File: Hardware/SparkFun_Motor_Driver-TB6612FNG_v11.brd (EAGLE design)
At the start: 20.3 x 20.3 mm, 14 parts, among them U1 TB6612FNG

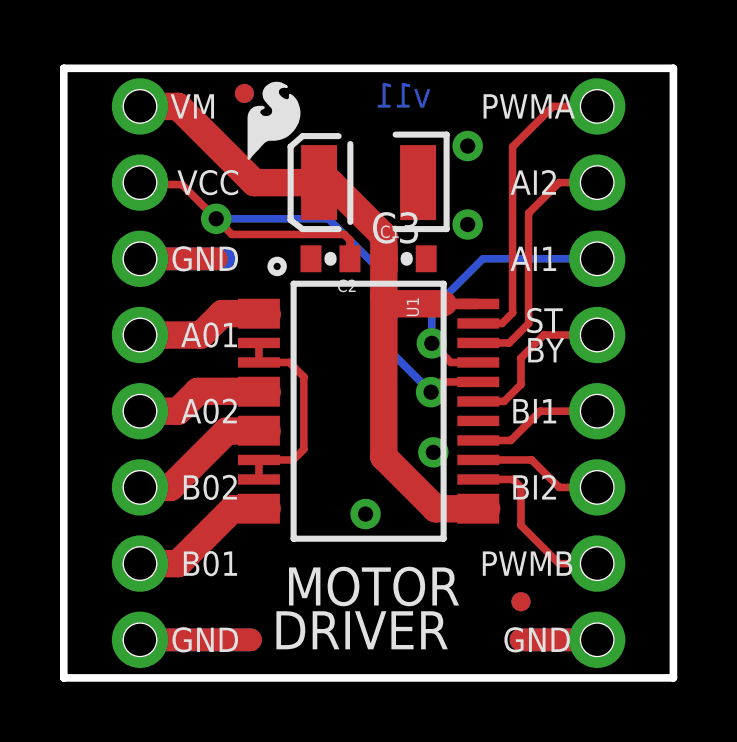
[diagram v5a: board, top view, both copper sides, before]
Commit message: Changed cap parts and added measures
-Replaced 0603 caps with caps from the sparkfun-capacitors lbr
-Replaced 10uf cap with cap from the sparkfun-capacitors lbr
-added measures to the design
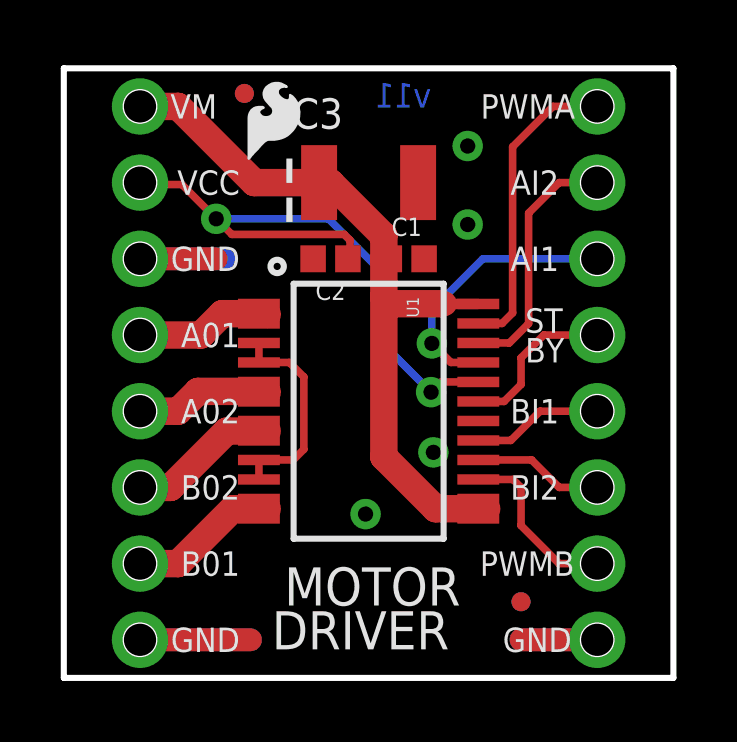
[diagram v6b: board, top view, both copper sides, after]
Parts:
- C1, C2: device SparkFun:0402-CAP -> SparkFun-Capacitors:0402
- C3: value 10uf , 20V -> 10uF; device SparkFun:EIA3528 -> SparkFun-Capacitors:EIA3528
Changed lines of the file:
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@@
 <setting verticaltext="up"/>
 </settings>
-<grid distance="0.05" unitdist="inch" unit="inch" style="lines" multiple="1" display="yes" altdistance="0.005" altunitdist="inch" altunit="inch"/>
+<grid distance="0.05" unitdist="inch" unit="inch" style="lines" multiple="1" display="yes" altdistance="0.0025" altunitdist="inch" altunit="inch"/>
 <layers>
 <layer number="1" name="Top" color="4" fill="1" visible="yes" active="yes"/>
@@
 <layer number="20" name="Dimension" color="15" fill="1" visible="yes" active="yes"/>
 <layer number="21" name="tPlace" color="16" fill="1" visible="yes" active="yes"/>
-<layer number="22" name="bPlace" color="14" fill="1" visible="no" active="yes"/>
+<layer number="22" name="bPlace" color="14" fill="1" visible="yes" active="yes"/>
 <layer number="23" name="tOrigins" color="15" fill="1" visible="yes" active="yes"/>
-<layer number="24" name="bOrigins" color="15" fill="1" visible="no" active="yes"/>
-<layer number="25" name="tNames" color="7" fill="1" visible="yes" active="yes"/>
+<layer number="24" name="bOrigins" color="15" fill="1" visible="yes" active="yes"/>
+<layer number="25" name="tNames" color="7" fill="1" visible="no" active="yes"/>
 <layer number="26" name="bNames" color="7" fill="1" visible="no" active="yes"/>
 <layer number="27" name="tValues" color="7" fill="1" visible="no" active="yes"/>
@@
 <layer number="42" name="bRestrict" color="1" fill="10" visible="no" active="yes"/>
 <layer number="43" name="vRestrict" color="2" fill="10" visible="no" active="yes"/>
-<layer number="44" name="Drills" color="7" fill="1" visible="yes" active="yes"/>
+<layer number="44" name="Drills" color="7" fill="1" visible="no" active="yes"/>
 <layer number="45" name="Holes" color="7" fill="1" visible="yes" active="yes"/>
 <layer number="46" name="Milling" color="3" fill="1" visible="no" active="yes"/>
-<layer number="47" name="Measures" color="7" fill="1" visible="no" active="yes"/>
-<layer number="48" name="Document" color="7" fill="1" visible="no" active="yes"/>
-<layer number="49" name="Reference" color="13" fill="1" visible="no" active="yes"/>
+<layer number="47" name="Measures" color="7" fill="1" visible="yes" active="yes"/>
+<layer number="48" name="Document" color="7" fill="1" visible="yes" active="yes"/>
+<layer number="49" name="Reference" color="13" fill="1" visible="yes" active="yes"/>
 <layer number="50" name="dxf" color="7" fill="1" visible="no" active="yes"/>
-<layer number="51" name="tDocu" color="6" fill="1" visible="no" active="yes"/>
+<layer number="51" name="tDocu" color="6" fill="1" visible="yes" active="yes"/>
 <layer number="52" name="bDocu" color="7" fill="1" visible="no" active="yes"/>
 <layer number="53" name="tGND_GNDA" color="7" fill="9" visible="no" active="no"/>
@@
 <layer number="225" name="225bmp" color="7" fill="1" visible="no" active="yes"/>
 <layer number="226" name="226bmp" color="7" fill="1" visible="no" active="yes"/>
-<layer number="227" name="LAYER_2" color="11" fill="1" visible="no" active="yes"/>
-<layer number="228" name="LAYER_3" color="10" fill="1" visible="no" active="yes"/>
-<layer number="229" name="LAYER_4" color="14" fill="1" visible="no" active="yes"/>
-<layer number="230" name="LAYER_5" color="12" fill="1" visible="no" active="yes"/>
-<layer number="231" name="LAYER_6" color="9" fill="1" visible="no" active="yes"/>
+<layer number="227" name="LAYER_2" color="11" fill="1" visible="yes" active="yes"/>
+<layer number="228" name="LAYER_3" color="10" fill="1" visible="yes" active="yes"/>
+<layer number="229" name="LAYER_4" color="14" fill="1" visible="yes" active="yes"/>
+<layer number="230" name="LAYER_5" color="12" fill="1" visible="yes" active="yes"/>
+<layer number="231" name="LAYER_6" color="9" fill="1" visible="yes" active="yes"/>
 <layer number="232" name="Eagle3D_PG2" color="7" fill="1" visible="no" active="yes"/>
 <layer number="233" name="Eagle3D_PG3" color="7" fill="1" visible="no" active="yes"/>
@@
 <board>
 <plain>
-<wire x1="0" y1="0" x2="20.32" y2="0" width="0.254" layer="20"/>
-<wire x1="20.32" y1="0" x2="20.32" y2="20.32" width="0.254" layer="20"/>
-<wire x1="20.32" y1="20.32" x2="0" y2="20.32" width="0.254" layer="20"/>
-<wire x1="0" y1="20.32" x2="0" y2="0" width="0.254" layer="20"/>
+<wire x1="0" y1="0" x2="20.32" y2="0" width="0.2032" layer="20"/>
+<wire x1="20.32" y1="0" x2="20.32" y2="20.32" width="0.2032" layer="20"/>
+<wire x1="20.32" y1="20.32" x2="0" y2="20.32" width="0.2032" layer="20"/>
+<wire x1="0" y1="20.32" x2="0" y2="0" width="0.2032" layer="20"/>
 <text x="3.5814" y="19.558" size="1.016" layer="22" font="vector" ratio="15" rot="MR180">VM</text>
 <text x="3.5814" y="17.018" size="1.016" layer="22" font="vector" ratio="15" rot="MR180">VCC</text>
@@
 <text x="-7.62" y="-15.24" size="1.778" layer="51" font="vector" ratio="10">Revised by:</text>
 <text x="12.7" y="-15.24" size="1.778" layer="51" font="vector" ratio="10">Eric Orosel</text>
+<dimension x1="0" y1="20.32" x2="20.32" y2="20.32" x3="10.16" y3="26.67" textsize="1.778" textratio="15" layer="47" unit="inch"/>
+<dimension x1="2.54" y1="19.05" x2="17.78" y2="19.05" x3="10.16" y3="22.86" textsize="1.778" textratio="15" layer="47" unit="inch"/>
+<dimension x1="0" y1="20.32" x2="0" y2="0" x3="-6.35" y3="10.16" textsize="1.778" textratio="15" layer="47" unit="inch"/>
+<dimension x1="0" y1="20.32" x2="0" y2="19.05" x3="-2.54" y3="19.685" textsize="1.778" textratio="15" layer="47" unit="inch"/>
 </plain>
 <attributes>
@@
 <attribute name="VALUE" value="TB6612FNG" x="10.16" y="8.89" size="1.778" layer="27" rot="R270" display="off"/>
 </element>
-<element name="C1" library="SparkFun" package="0402-CAP" value="0.1uF" x="11.43" y="13.97"/>
-<element name="C2" library="SparkFun" package="0402-CAP" value="0.1uF" x="8.89" y="13.97" rot="R180"/>
-<element name="C3" library="SparkFun" package="EIA3528" value="10uf , 20V" x="10.16" y="16.51" smashed="yes" rot="R180">
-<attribute name="NAME" x="11.91" y="15.51" size="1.016" layer="25" rot="R180"/>
-<attribute name="VALUE" x="14.704" y="24.2" size="1.016" layer="27" rot="R180"/>
+<element name="C1" library="SparkFun-Capacitors" package="0402" value="0.1uF" x="11.43" y="13.97">
+<attribute name="PROD_ID" value="CAP-12416" x="11.43" y="13.97" size="1.778" layer="27" display="off"/>
+<attribute name="VALUE" value="0.1uF" x="11.43" y="13.97" size="1.778" layer="27" display="off"/>
+</element>
+<element name="C2" library="SparkFun-Capacitors" package="0402" value="0.1uF" x="8.89" y="13.97" rot="R180">
+<attribute name="PROD_ID" value="CAP-12416" x="8.89" y="13.97" size="1.778" layer="27" rot="R180" display="off"/>
+<attribute name="VALUE" value="0.1uF" x="8.89" y="13.97" size="1.778" layer="27" rot="R180" display="off"/>
+</element>
+<element name="C3" library="SparkFun-Capacitors" package="EIA3528" value="10uF" x="10.16" y="16.51" smashed="yes" rot="R180">
+<attribute name="NAME" x="9.3065" y="19.32" size="1.016" layer="25" rot="R180"/>
+<attribute name="VALUE" value="10uF" x="13.6245" y="19.3105" size="1.016" layer="27" rot="R180"/>
+<attribute name="PROD_ID" value="CAP-08063" x="10.16" y="16.51" size="1.778" layer="27" rot="R180" display="off"/>
 </element>
 <element name="JP1" library="Testing" package="1X08_OFFSET_REDUCED" value="" x="2.54" y="1.27" smashed="yes" rot="R90">
@@
 <wire x1="10.668" y1="14.732" x2="8.89" y2="16.51" width="0.9144" layer="1"/>
 <wire x1="10.668" y1="13.97" x2="10.668" y2="14.732" width="0.9144" layer="1"/>
-<wire x1="10.668" y1="13.97" x2="10.78" y2="13.97" width="0.254" layer="1"/>
+<wire x1="10.668" y1="13.97" x2="10.85" y2="13.97" width="0.254" layer="1"/>
 <wire x1="10.668" y1="7.366" x2="10.668" y2="12.7" width="0.9144" layer="1"/>
 <wire x1="10.668" y1="12.7" x2="10.668" y2="13.97" width="0.9144" layer="1"/>
@@
 <contactref element="JP1" pad="7"/>
 <contactref element="C2" pad="1"/>
-<wire x1="9.54" y1="13.97" x2="9.54" y2="14.59" width="0.254" layer="1"/>
 <wire x1="9.3472" y1="14.7828" x2="9.54" y2="14.59" width="0.254" layer="1"/>
 <wire x1="13.816" y1="9.865" x2="12.5828" y2="9.865" width="0.254" layer="1"/>
@@
 <wire x1="3.937" y1="16.4465" x2="2.6035" y2="16.4465" width="0.254" layer="1"/>
 <wire x1="2.6035" y1="16.4465" x2="2.54" y2="16.51" width="0.254" layer="1"/>
+<wire x1="9.54" y1="14.59" x2="9.54" y2="14.04" width="0.254" layer="1"/>
+<wire x1="9.54" y1="14.04" x2="9.47" y2="13.97" width="0.254" layer="1"/>
 </signal>
 <signal name="PWMA">
